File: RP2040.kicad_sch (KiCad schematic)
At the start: 27 parts, among them J1 USB_B_Micro, J2 Conn_01x02, J3 RP2040_SWD, U1 RP2040, U2 AMS1117-3.3, U3 W25Q128JVS, Y1 X322512MSB4SI

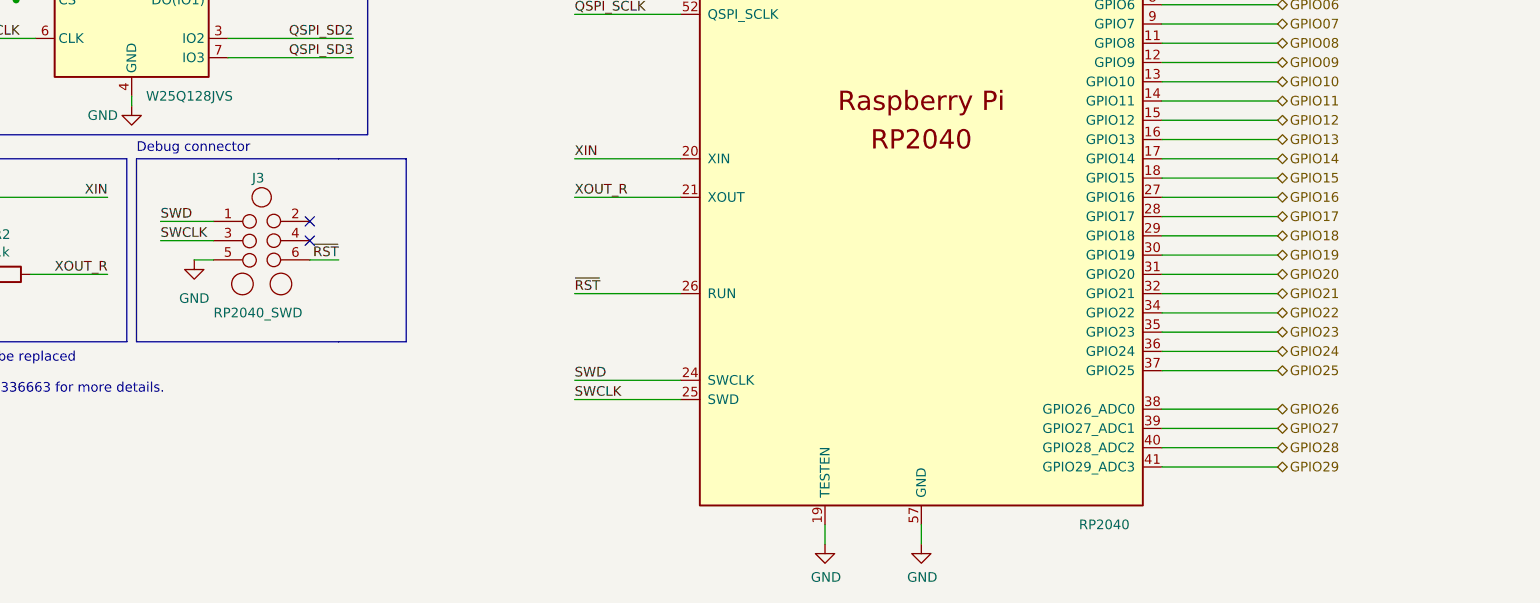
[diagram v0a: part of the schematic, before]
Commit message: All the buttons are routed. Ugly, but routed.
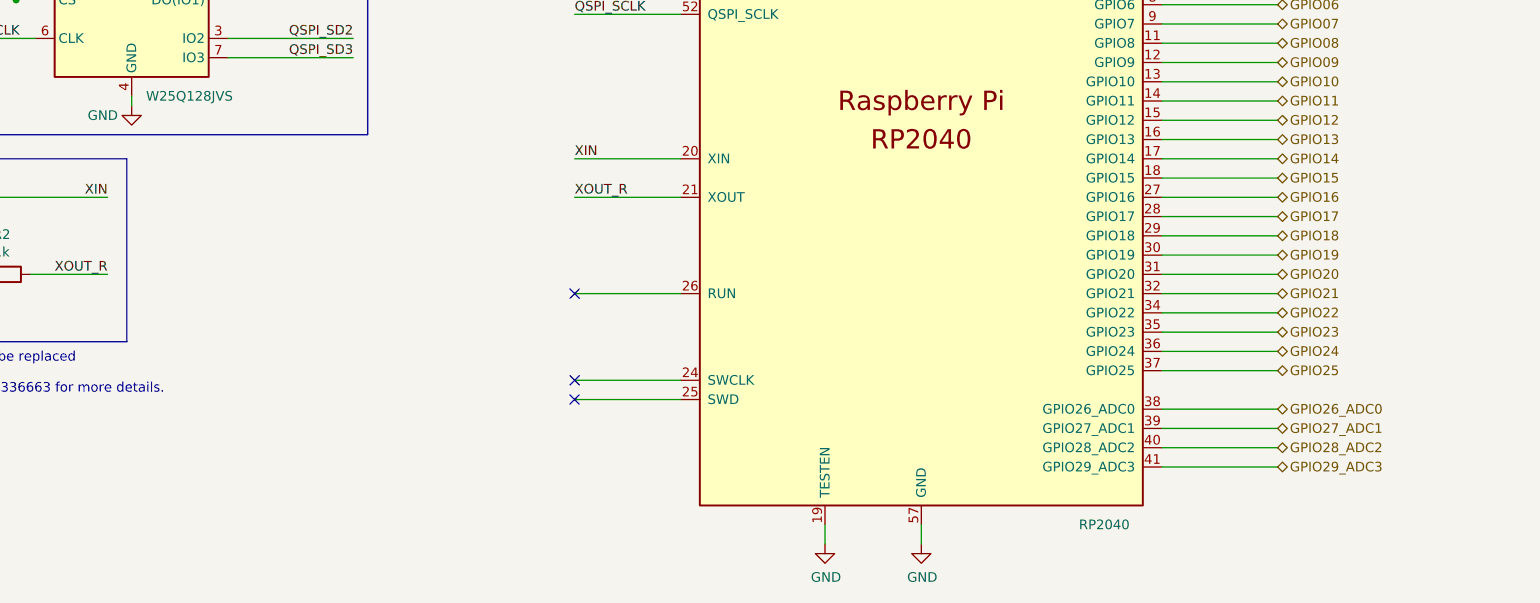
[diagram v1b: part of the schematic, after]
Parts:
- removed J3: RP2040_SWD, Connector:Tag-Connect_TC2030-IDC-NL_2x03_P1.27mm_Vertical, symbol Custom_Symbols:TC2030-IDC-NL
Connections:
- net GPIO26 renamed GPIO26_ADC0
- net GPIO27 renamed GPIO27_ADC1
- net GPIO28 renamed GPIO28_ADC2
- net GPIO29 renamed GPIO29_ADC3
- net SWCLK: no longer names the net of U1.25 (SWD)
- net SWD: no longer names the net of U1.24 (SWCLK)
- net ~{RST}: no longer names the net of U1.26 (RUN)
- no-connect marks 3 -> 4
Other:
- note removed: "Debug connector"
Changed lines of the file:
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@@
   (junction (at 194.945 40.005) (diameter 0) (color 0 0 0 0)
   )
-  (no_connect (at 97.79 114.3))
-  (no_connect (at 97.79 116.84))
+  (no_connect (at 132.715 123.825))
+  (no_connect (at 132.715 135.255))
+  (no_connect (at 132.715 137.795))
   (no_connect (at 29.21 34.29))
   (wire (pts (xy 139.065 20.955) (xy 139.065 19.685))
@@
     (stroke (width 0) (type default) (color 0 0 0 0))
   )
-  (polyline (pts (xy 74.93 106.045) (xy 101.6 106.045))
-    (stroke (width 0) (type default) (color 0 0 0 0))
-  )
   (wire (pts (xy 238.125 20.955) (xy 238.125 19.685))
     (stroke (width 0) (type default) (color 0 0 0 0))
@@
     (stroke (width 0) (type default) (color 0 0 0 0))
   )
-  (wire (pts (xy 82.55 119.38) (xy 85.09 119.38))
-    (stroke (width 0) (type default) (color 0 0 0 0))
-  )
   (wire (pts (xy 132.715 80.645) (xy 146.685 80.645))
     (stroke (width 0) (type default) (color 0 0 0 0))
@@
     (stroke (width 0) (type default) (color 0 0 0 0))
   )
-  (polyline (pts (xy 74.93 106.045) (xy 74.93 130.175))
-    (stroke (width 0) (type default) (color 0 0 0 0))
-  )
   (wire (pts (xy 210.185 80.645) (xy 225.425 80.645))
     (stroke (width 0) (type default) (color 0 0 0 0))
@@
     (stroke (width 0) (type default) (color 0 0 0 0))
   )
-  (polyline (pts (xy 110.49 106.045) (xy 110.49 130.175))
-    (stroke (width 0) (type default) (color 0 0 0 0))
-  )
   (wire (pts (xy 260.985 31.115) (xy 272.415 31.115))
     (stroke (width 0) (type default) (color 0 0 0 0))
@@
     (stroke (width 0) (type default) (color 0 0 0 0))
   )
-  (wire (pts (xy 78.105 116.84) (xy 85.09 116.84))
-    (stroke (width 0) (type default) (color 0 0 0 0))
-  )
   (wire (pts (xy 210.185 73.025) (xy 225.425 73.025))
     (stroke (width 0) (type default) (color 0 0 0 0))
@@
     (stroke (width 0) (type default) (color 0 0 0 0))
   )
-  (wire (pts (xy 97.79 119.38) (xy 101.6 119.38))
-    (stroke (width 0) (type default) (color 0 0 0 0))
-  )
   (wire (pts (xy 86.995 82.55) (xy 103.505 82.55))
     (stroke (width 0) (type default) (color 0 0 0 0))
@@
     (stroke (width 0) (type default) (color 0 0 0 0))
   )
-  (wire (pts (xy 78.105 114.3) (xy 85.09 114.3))
-    (stroke (width 0) (type default) (color 0 0 0 0))
-  )
   (polyline (pts (xy 13.97 52.705) (xy 13.97 102.87))
     (stroke (width 0) (type default) (color 0 0 0 0))
@@
     (stroke (width 0) (type default) (color 0 0 0 0))
   )
-  (polyline (pts (xy 101.6 106.045) (xy 110.49 106.045))
-    (stroke (width 0) (type default) (color 0 0 0 0))
-  )
   (wire (pts (xy 260.985 28.575) (xy 260.985 31.115))
     (stroke (width 0) (type default) (color 0 0 0 0))
@@
     (stroke (width 0) (type default) (color 0 0 0 0))
   )
-  (polyline (pts (xy 74.93 130.175) (xy 101.6 130.175))
-    (stroke (width 0) (type default) (color 0 0 0 0))
-  )
   (wire (pts (xy 158.115 40.005) (xy 158.115 52.705))
     (stroke (width 0) (type default) (color 0 0 0 0))
@@
   )
   (wire (pts (xy 158.115 19.685) (xy 158.115 40.005))
-    (stroke (width 0) (type default) (color 0 0 0 0))
-  )
-  (polyline (pts (xy 110.49 130.175) (xy 101.6 130.175))
     (stroke (width 0) (type default) (color 0 0 0 0))
   )
@@
     (effects (font (size 1.27 1.27)) (justify left bottom))
   )
-  (text "Debug connector" (at 74.93 105.41 0)
-    (effects (font (size 1.27 1.27)) (justify left bottom))
-  )
   (text "If there are stability issues then R4 may need to be replaced\nwith a smaller value resistor. See \nhttps://forums.raspberrypi.com/viewtopic.php?t=336663 for more details."
     (at 13.97 137.16 0)
@@
     (effects (font (size 1.27 1.27)) (justify left bottom))
   )
-  (label "SWCLK" (at 78.105 116.84 0)
-    (effects (font (size 1.27 1.27)) (justify left bottom))
-  )
   (label "XOUT" (at 46.355 121.285 0)
     (effects (font (size 1.27 1.27)) (justify left bottom))
@@
     (effects (font (size 1.27 1.27)) (justify right bottom))
   )
-  (label "SWD" (at 132.715 135.255 0)
-    (effects (font (size 1.27 1.27)) (justify left bottom))
-  )
   (label "QSPI_SD0" (at 132.715 75.565 0)
     (effects (font (size 1.27 1.27)) (justify left bottom))
@@
     (effects (font (size 1.27 1.27)) (justify left bottom))
   )
-  (label "SWD" (at 78.105 114.3 0)
-    (effects (font (size 1.27 1.27)) (justify left bottom))
-  )
   (label "QSPI_SD1" (at 103.505 85.09 180)
     (effects (font (size 1.27 1.27)) (justify right bottom))
@@
     (effects (font (size 1.27 1.27)) (justify left bottom))
   )
-  (label "~{RST}" (at 101.6 119.38 180)
-    (effects (font (size 1.27 1.27)) (justify right bottom))
-  )
   (label "QSPI_SCLK" (at 50.165 90.17 0)
     (effects (font (size 1.27 1.27)) (justify left bottom))
@@
     (effects (font (size 1.27 1.27)) (justify right bottom))
   )
-  (label "SWCLK" (at 132.715 137.795 0)
-    (effects (font (size 1.27 1.27)) (justify left bottom))
-  )
   (label "QSPI_SS" (at 50.165 85.09 0)
     (effects (font (size 1.27 1.27)) (justify left bottom))
@@
   )
   (label "~{USB_BOOT}" (at 27.305 85.09 0)
-    (effects (font (size 1.27 1.27)) (justify left bottom))
-  )
-  (label "~{RST}" (at 132.715 123.825 0)
     (effects (font (size 1.27 1.27)) (justify left bottom))
   )
@@
     (effects (font (size 1.27 1.27)) (justify right bottom))
   )
-  (hierarchical_label "GPIO26" (shape bidirectional) (at 225.425 139.065 0)
+  (hierarchical_label "GPIO26_ADC0" (shape bidirectional) (at 225.425 139.065 0)
     (effects (font (size 1.27 1.27)) (justify left))
   )
@@
     (effects (font (size 1.27 1.27)) (justify left))
   )
-  (hierarchical_label "GPIO27" (shape bidirectional) (at 225.425 141.605 0)
-    (effects (font (size 1.27 1.27)) (justify left))
-  )
-  (hierarchical_label "GPIO29" (shape bidirectional) (at 225.425 146.685 0)
+  (hierarchical_label "GPIO27_ADC1" (shape bidirectional) (at 225.425 141.605 0)
+    (effects (font (size 1.27 1.27)) (justify left))
+  )
+  (hierarchical_label "GPIO29_ADC3" (shape bidirectional) (at 225.425 146.685 0)
     (effects (font (size 1.27 1.27)) (justify left))
   )
@@
     (effects (font (size 1.27 1.27)) (justify left))
   )
-  (hierarchical_label "GPIO28" (shape bidirectional) (at 225.425 144.145 0)
+  (hierarchical_label "GPIO28_ADC2" (shape bidirectional) (at 225.425 144.145 0)
     (effects (font (size 1.27 1.27)) (justify left))
   )
@@
     (pin "3")
     (pin "4")
-  )
-  (symbol (lib_id "Custom_Symbols:TC2030-IDC-NL") (at 91.44 116.84 0) (unit 1)
-    (in_bom yes) (on_board yes)
-    (property "Reference" "J3" (id 0) (at 90.17 108.585 0)
-      (effects (font (size 1.27 1.27)) (justify left))
-    )
-    (property "Value" "RP2040_SWD" (id 1) (at 85.09 126.365 0)
-      (effects (font (size 1.27 1.27)) (justify left))
-    )
-    (property "Footprint" "Connector:Tag-Connect_TC2030-IDC-NL_2x03_P1.27mm_Vertical" (id 2) (at 90.17 116.84 0)
-      (effects (font (size 1.27 1.27)) hide)
-    )
-    (property "Datasheet" "https://www.tag-connect.com/wp-content/uploads/bsk-pdf-manager/2019/12/TC2030-IDC-NL-Datasheet-Rev-B.pdf" (id 3) (at 91.44 130.81 0)
-      (effects (font (size 1.27 1.27)) hide)
-    )
-    (pin "1")
-    (pin "2")
-    (pin "3")
-    (pin "4")
-    (pin "5")
-    (pin "6")
   )
   (symbol (lib_id "Custom_Symbols:RP2040") (at 178.435 103.505 0) (unit 1)
@@
     (pin "2")
   )
-  (symbol (lib_id "power:GND") (at 82.55 119.38 0) (unit 1)
-    (in_bom yes) (on_board yes) (fields_autoplaced)
-    (property "Reference" "#PWR0116" (id 0) (at 82.55 125.73 0)
-      (effects (font (size 1.27 1.27)) hide)
-    )
-    (property "Value" "GND" (id 1) (at 82.55 124.46 0))
-    (property "Footprint" "" (id 2) (at 82.55 119.38 0)
-      (effects (font (size 1.27 1.27)) hide)
-    )
-    (property "Datasheet" "" (id 3) (at 82.55 119.38 0)
-      (effects (font (size 1.27 1.27)) hide)
-    )
-    (pin "1")
-  )
   (symbol (lib_id "Device:C") (at 149.225 24.765 0) (unit 1)
